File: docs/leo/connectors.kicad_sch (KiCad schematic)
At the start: 9 parts, among them CN1_A Conn_01x32, CN1_B Conn_01x32, CN1_C Conn_01x32, CN2_A Conn_01x32, CN2_B Conn_01x32, CN2_C Conn_01x32, CN3_A Conn_01x32, CN3_B Conn_01x32

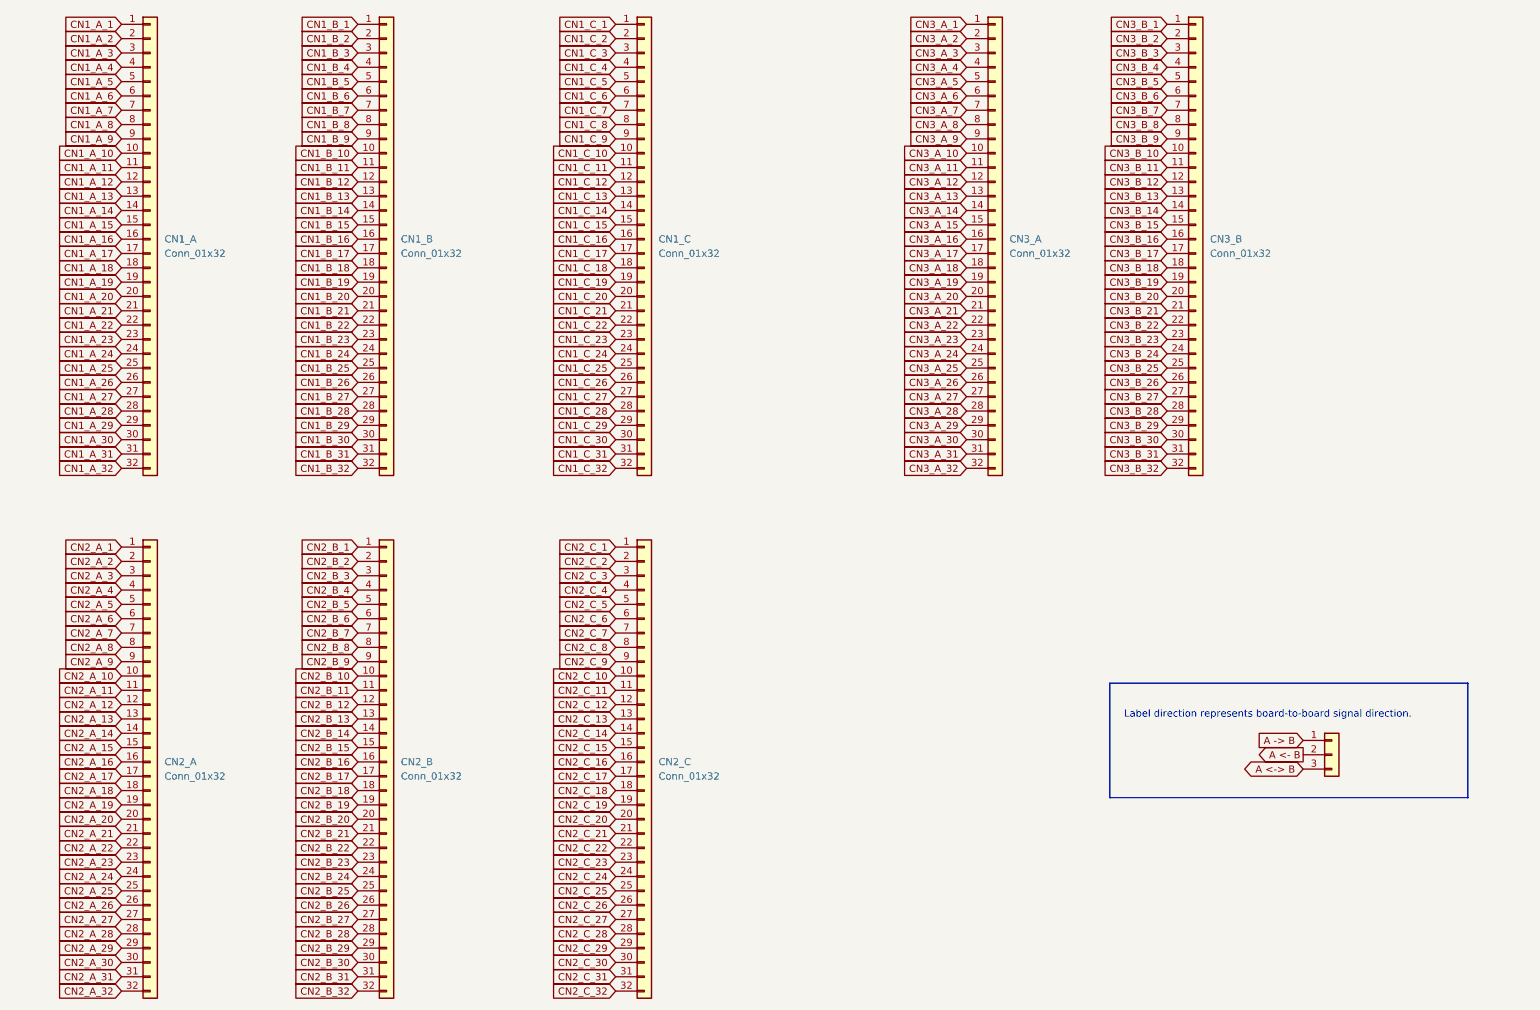
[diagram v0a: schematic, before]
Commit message: Name most of the CN1 and CN2 pins
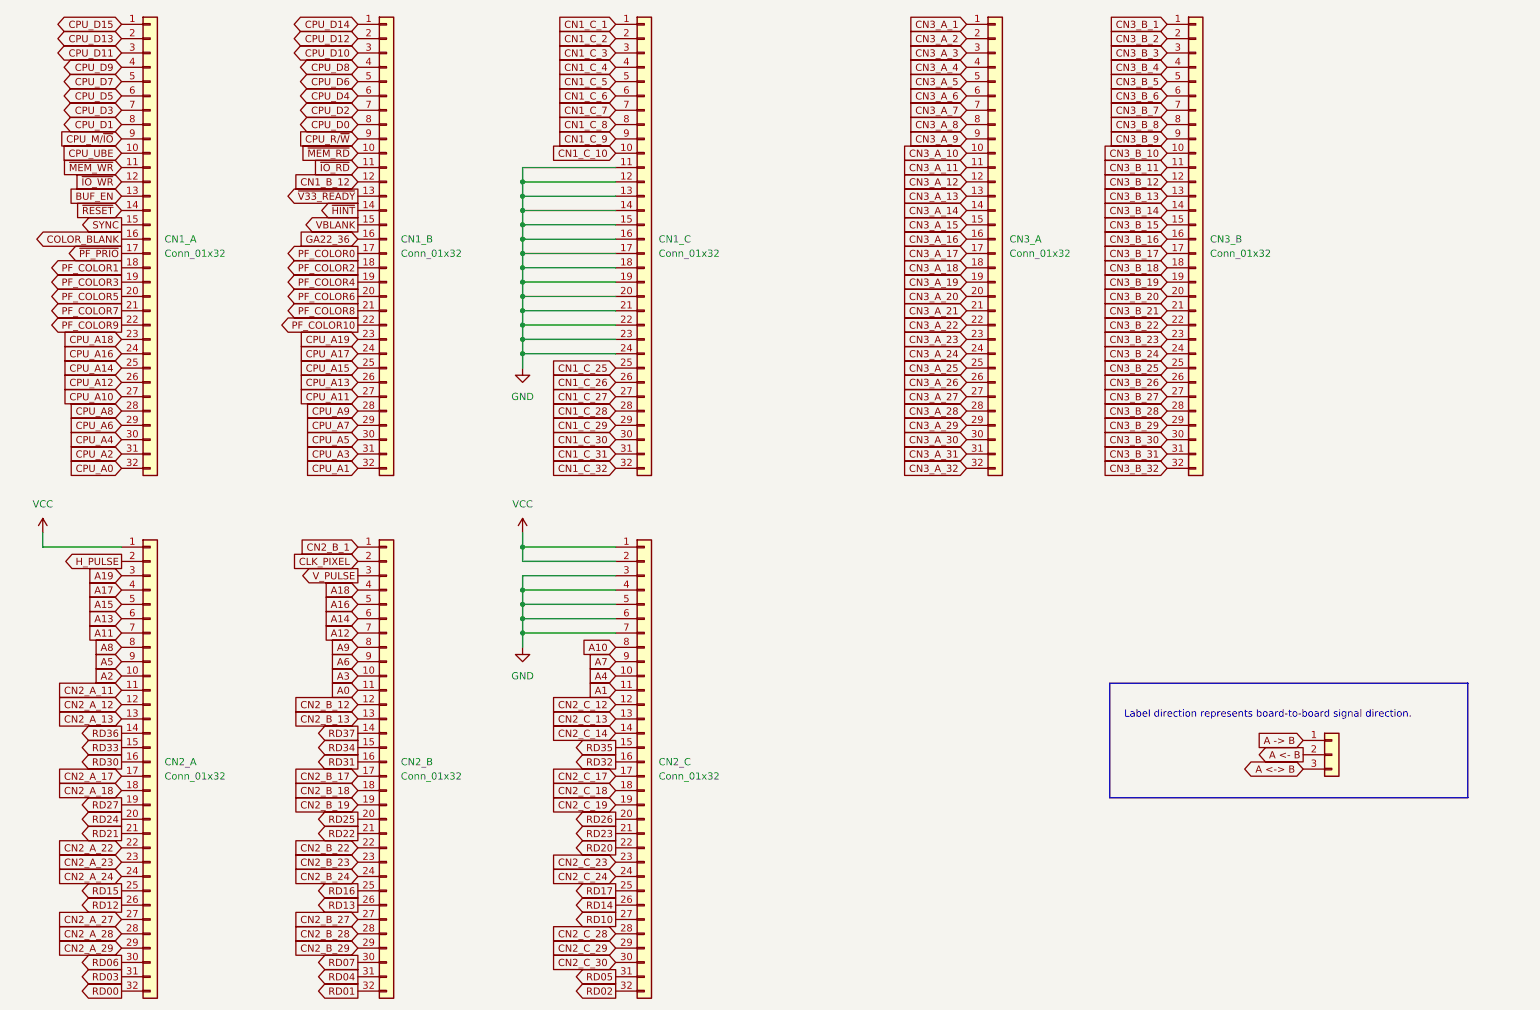
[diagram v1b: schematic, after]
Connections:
- net CN1_C_12 is gone; now on net GND: CN1_C.12 (Pin_12)
- net CN1_C_13 is gone; now on net GND: CN1_C.13 (Pin_13)
- net CN1_C_14 is gone; now on net GND: CN1_C.14 (Pin_14)
- net CN1_C_15 is gone; now on net GND: CN1_C.15 (Pin_15)
- net CN1_C_16 is gone; now on net GND: CN1_C.16 (Pin_16)
- net CN1_C_17 is gone; now on net GND: CN1_C.17 (Pin_17)
- net CN1_C_18 is gone; now on net GND: CN1_C.18 (Pin_18)
- net CN1_C_19 is gone; now on net GND: CN1_C.19 (Pin_19)
- net CN1_C_20 is gone; now on net GND: CN1_C.20 (Pin_20)
- net CN1_C_21 is gone; now on net GND: CN1_C.21 (Pin_21)
- net CN1_C_22 is gone; now on net GND: CN1_C.22 (Pin_22)
- net CN1_C_23 is gone; now on net GND: CN1_C.23 (Pin_23)
- net CN1_C_24 is gone; now on net GND: CN1_C.24 (Pin_24)
- net CN2_C_1 is gone; now on net VCC: CN2_C.1 (Pin_1)
- net CN2_C_2 is gone; now on net VCC: CN2_C.2 (Pin_2)
- net CN2_C_3 is gone; now on net GND: CN2_C.3 (Pin_3)
- net CN2_C_4 is gone; now on net GND: CN2_C.4 (Pin_4)
- net CN2_C_5 is gone; now on net GND: CN2_C.5 (Pin_5)
- net CN2_C_6 is gone; now on net GND: CN2_C.6 (Pin_6)
- net CN2_C_7 is gone; now on net GND: CN2_C.7 (Pin_7)
- net CN1_A_1 renamed CPU_D15
- net CN1_A_10 renamed CPU_UBE
- net CN1_A_11 renamed ~{MEM_WR}
- net CN1_A_12 renamed ~{IO_WR}
- net CN1_A_13 renamed BUF_EN
- net CN1_A_14 renamed ~{RESET}
- net CN1_A_15 renamed SYNC
- net CN1_A_16 renamed COLOR_BLANK
- net CN1_A_17 renamed ~{PF_PRIO}
- net CN1_A_18 renamed PF_COLOR1
- net CN1_A_19 renamed PF_COLOR3
- net CN1_A_2 renamed CPU_D13
- net CN1_A_20 renamed PF_COLOR5
- net CN1_A_21 renamed PF_COLOR7
- net CN1_A_22 renamed PF_COLOR9
- net CN1_A_23 renamed CPU_A18
- net CN1_A_24 renamed CPU_A16
- net CN1_A_25 renamed CPU_A14
- net CN1_A_26 renamed CPU_A12
- net CN1_A_27 renamed CPU_A10
- net CN1_A_28 renamed CPU_A8
- net CN1_A_29 renamed CPU_A6
- net CN1_A_3 renamed CPU_D11
- net CN1_A_30 renamed CPU_A4
- net CN1_A_31 renamed CPU_A2
- net CN1_A_32 renamed CPU_A0
- net CN1_A_4 renamed CPU_D9
- net CN1_A_5 renamed CPU_D7
- net CN1_A_6 renamed CPU_D5
- net CN1_A_7 renamed CPU_D3
- net CN1_A_8 renamed CPU_D1
- net CN1_A_9 renamed CPU_M/~{IO}
- net CN1_B_1 renamed CPU_D14
- net CN1_B_10 renamed ~{MEM_RD}
- net CN1_B_11 renamed ~{IO_RD}
- net CN1_B_13 renamed ~{V33_READY}
- net CN1_B_14 renamed ~{HINT}
- net CN1_B_15 renamed VBLANK
- net CN1_B_16 renamed GA22_36
- net CN1_B_17 renamed PF_COLOR0
- net CN1_B_18 renamed PF_COLOR2
- net CN1_B_19 renamed PF_COLOR4
- net CN1_B_2 renamed CPU_D12
- net CN1_B_20 renamed PF_COLOR6
- net CN1_B_21 renamed PF_COLOR8
- net CN1_B_22 renamed PF_COLOR10
- net CN1_B_23 renamed CPU_A19
- net CN1_B_24 renamed CPU_A17
- net CN1_B_25 renamed CPU_A15
- net CN1_B_26 renamed CPU_A13
- net CN1_B_27 renamed CPU_A11
- net CN1_B_28 renamed CPU_A9
- net CN1_B_29 renamed CPU_A7
- net CN1_B_3 renamed CPU_D10
- net CN1_B_30 renamed CPU_A5
- net CN1_B_31 renamed CPU_A3
- net CN1_B_32 renamed CPU_A1
- net CN1_B_4 renamed CPU_D8
- net CN1_B_5 renamed CPU_D6
- net CN1_B_6 renamed CPU_D4
- net CN1_B_7 renamed CPU_D2
- net CN1_B_8 renamed CPU_D0
- net CN1_B_9 renamed CPU_R/~{W}
- net CN1_C_11 renamed GND
- net CN2_A_1 renamed VCC
- net CN2_A_10 renamed A2
- net CN2_A_14 renamed RD36
- net CN2_A_15 renamed RD33
- net CN2_A_16 renamed RD30
- net CN2_A_19 renamed RD27
- net CN2_A_2 renamed H_PULSE
- net CN2_A_20 renamed RD24
- net CN2_A_21 renamed RD21
- net CN2_A_25 renamed RD15
- net CN2_A_26 renamed RD12
- net CN2_A_3 renamed A19
- net CN2_A_30 renamed RD06
- net CN2_A_31 renamed RD03
- net CN2_A_32 renamed RD00
- net CN2_A_4 renamed A17
- net CN2_A_5 renamed A15
- net CN2_A_6 renamed A13
- net CN2_A_7 renamed A11
- net CN2_A_8 renamed A8
- net CN2_A_9 renamed A5
- net CN2_B_10 renamed A3
- net CN2_B_11 renamed A0
- net CN2_B_14 renamed RD37
- net CN2_B_15 renamed RD34
- net CN2_B_16 renamed RD31
- net CN2_B_2 renamed CLK_PIXEL
- net CN2_B_20 renamed RD25
- net CN2_B_21 renamed RD22
- net CN2_B_25 renamed RD16
- net CN2_B_26 renamed RD13
- net CN2_B_3 renamed V_PULSE
- net CN2_B_30 renamed RD07
- net CN2_B_31 renamed RD04
- net CN2_B_32 renamed RD01
- net CN2_B_4 renamed A18
- net CN2_B_5 renamed A16
- net CN2_B_6 renamed A14
- net CN2_B_7 renamed A12
- net CN2_B_8 renamed A9
- net CN2_B_9 renamed A6
- net CN2_C_10 renamed A4
- net CN2_C_11 renamed A1
- net CN2_C_15 renamed RD35
- net CN2_C_16 renamed RD32
- net CN2_C_20 renamed RD26
- net CN2_C_21 renamed RD23
- net CN2_C_22 renamed RD20
- net CN2_C_25 renamed RD17
- net CN2_C_26 renamed RD14
- net CN2_C_27 renamed RD10
- net CN2_C_31 renamed RD05
- net CN2_C_32 renamed RD02
- net CN2_C_8 renamed A10
- net CN2_C_9 renamed A7

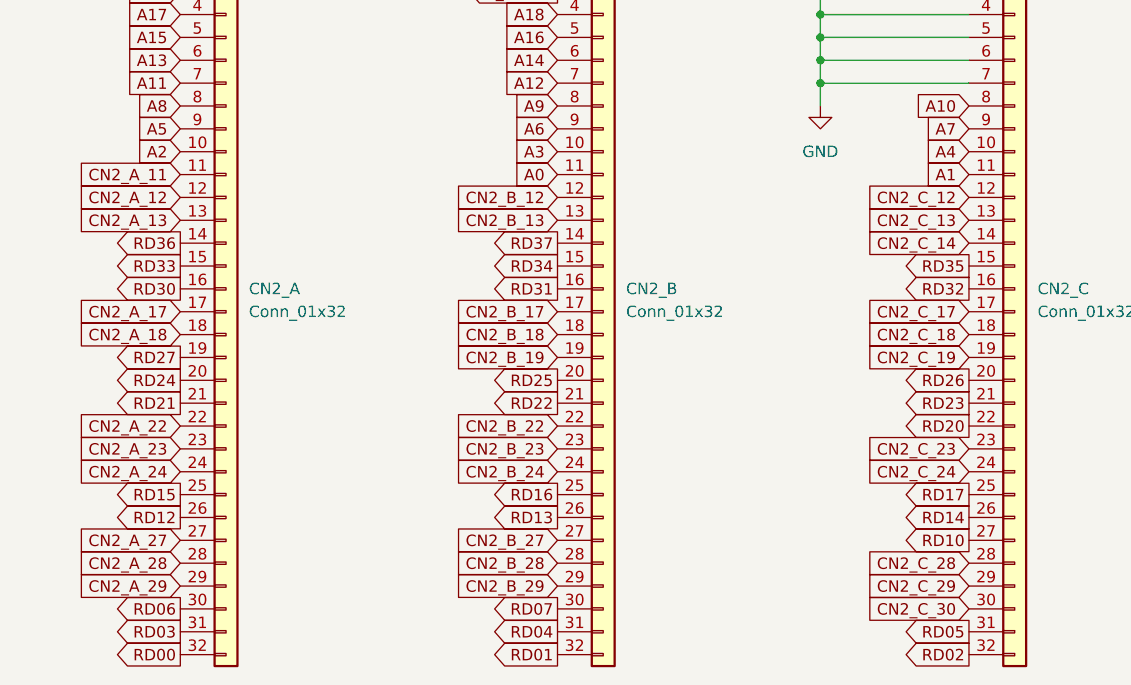
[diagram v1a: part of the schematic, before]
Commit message: Fill in word data signals based on pattern
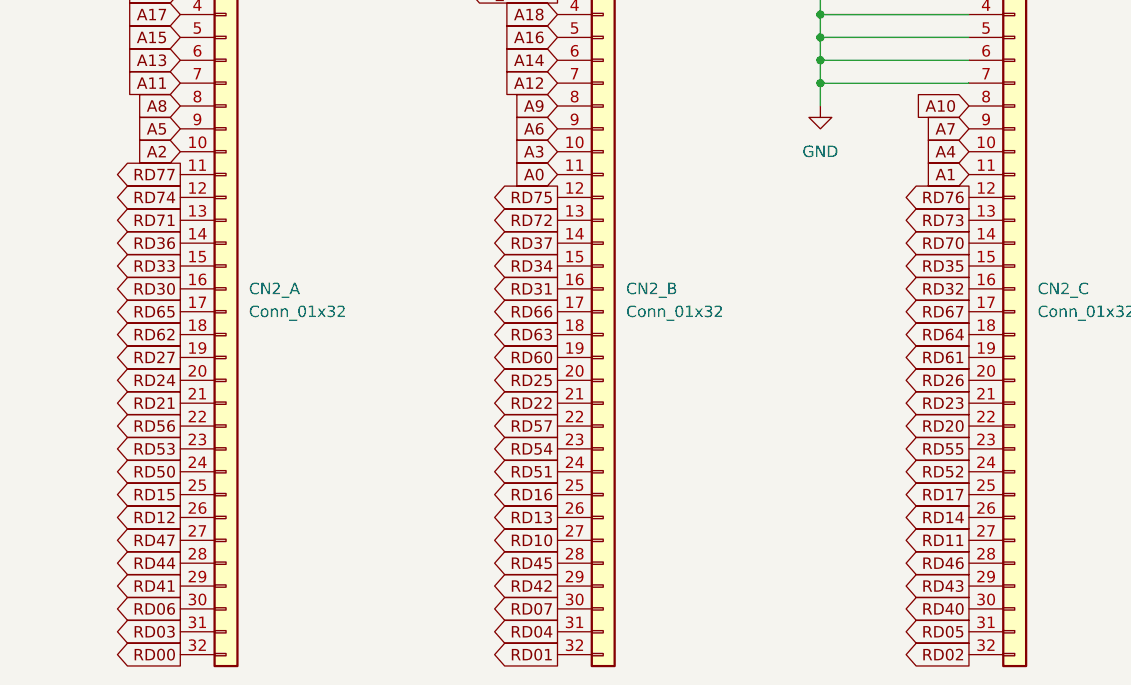
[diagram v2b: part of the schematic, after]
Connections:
- net CN2_B_27 is gone; now on net RD10: CN2_B.27 (Pin_27)
- net RD10: no longer CN2_C.27 (Pin_27)
- net CN2_A_11 renamed RD77
- net CN2_A_12 renamed RD74
- net CN2_A_13 renamed RD71
- net CN2_A_17 renamed RD65
- net CN2_A_18 renamed RD62
- net CN2_A_22 renamed RD56
- net CN2_A_23 renamed RD53
- net CN2_A_24 renamed RD50
- net CN2_A_27 renamed RD47
- net CN2_A_28 renamed RD44
- net CN2_A_29 renamed RD41
- net CN2_B_12 renamed RD75
- net CN2_B_13 renamed RD72
- net CN2_B_17 renamed RD66
- net CN2_B_18 renamed RD63
- net CN2_B_19 renamed RD60
- net CN2_B_22 renamed RD57
- net CN2_B_23 renamed RD54
- net CN2_B_24 renamed RD51
- net CN2_B_28 renamed RD45
- net CN2_B_29 renamed RD42
- net CN2_C_12 renamed RD76
- net CN2_C_13 renamed RD73
- net CN2_C_14 renamed RD70
- net CN2_C_17 renamed RD67
- net CN2_C_18 renamed RD64
- net CN2_C_19 renamed RD61
- net CN2_C_23 renamed RD55
- net CN2_C_24 renamed RD52
- net CN2_C_28 renamed RD46
- net CN2_C_29 renamed RD43
- net CN2_C_30 renamed RD40
- new net RD11: CN2_C.27 (Pin_27)
